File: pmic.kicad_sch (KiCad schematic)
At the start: 38 parts, among them J401 Conn_01x04, J402 EMI shield frame, U401 STPMIC1DPQR

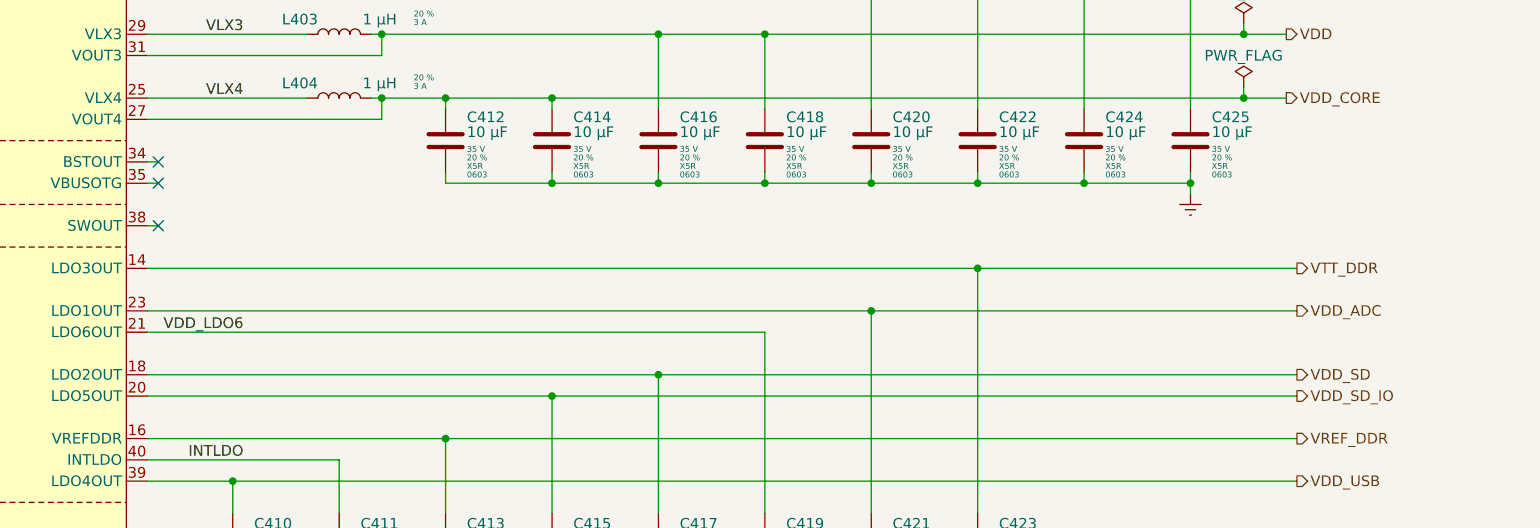
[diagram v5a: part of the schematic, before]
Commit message: Fallback to DDR series termination
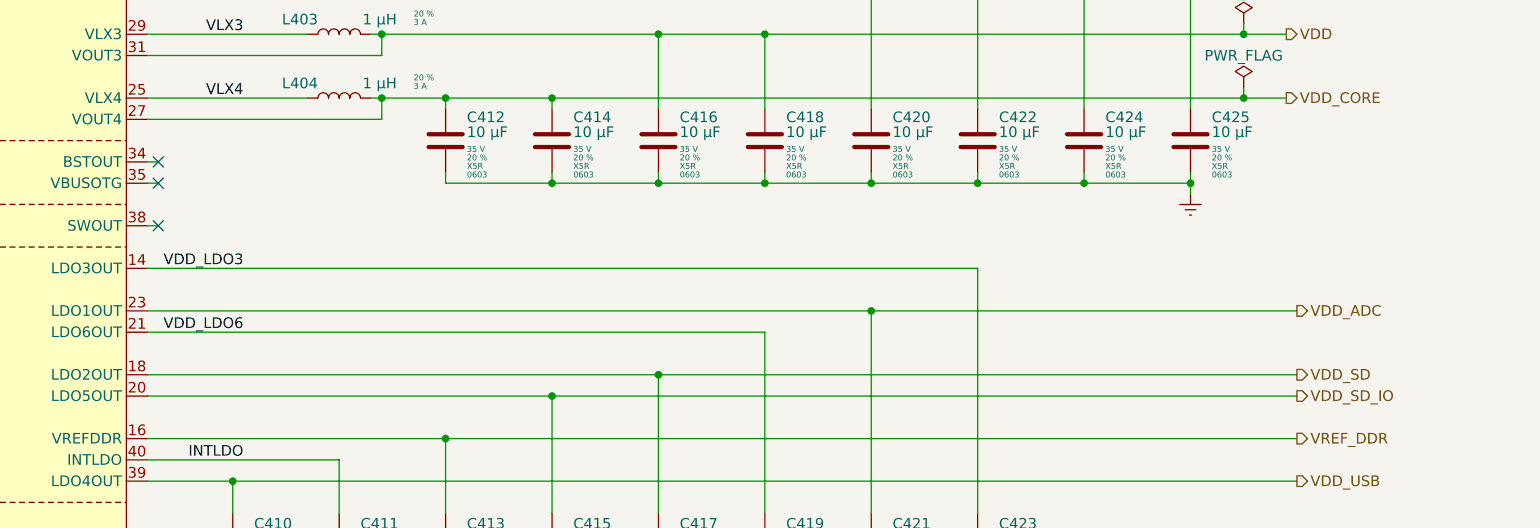
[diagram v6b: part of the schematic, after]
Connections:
- net VTT_DDR renamed VDD_LDO3
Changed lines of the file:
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@@
-	)
-	(junction
-		(at 292.1 157.48)
-		(diameter 0)
-		(color 0 0 0 0)
 	)
 	(junction
@@
 		(pts
 			(xy 133.35 114.3) (xy 133.35 116.84)
-		)
-		(stroke
-			(width 0)
-			(type default)
-		)
-	)
-	(wire
-		(pts
-			(xy 292.1 157.48) (xy 330.2 157.48)
 		)
 		(stroke
@@
 	(label "VLX2"
 		(at 204.47 121.92 180)
+		(effects
+			(font
+				(size 1.27 1.27)
+			)
+			(justify right bottom)
+		)
+	)
+	(label "VDD_LDO3"
+		(at 204.47 157.48 180)
 		(effects
 			(font
@@
 		(effects
 			(font
-				(size 1.27 1.27)
-			)
-			(justify left)
-		)
-	)
-	(hierarchical_label "VTT_DDR"
-		(shape output)
-		(at 330.2 157.48 0)
-		(effects
-			(font

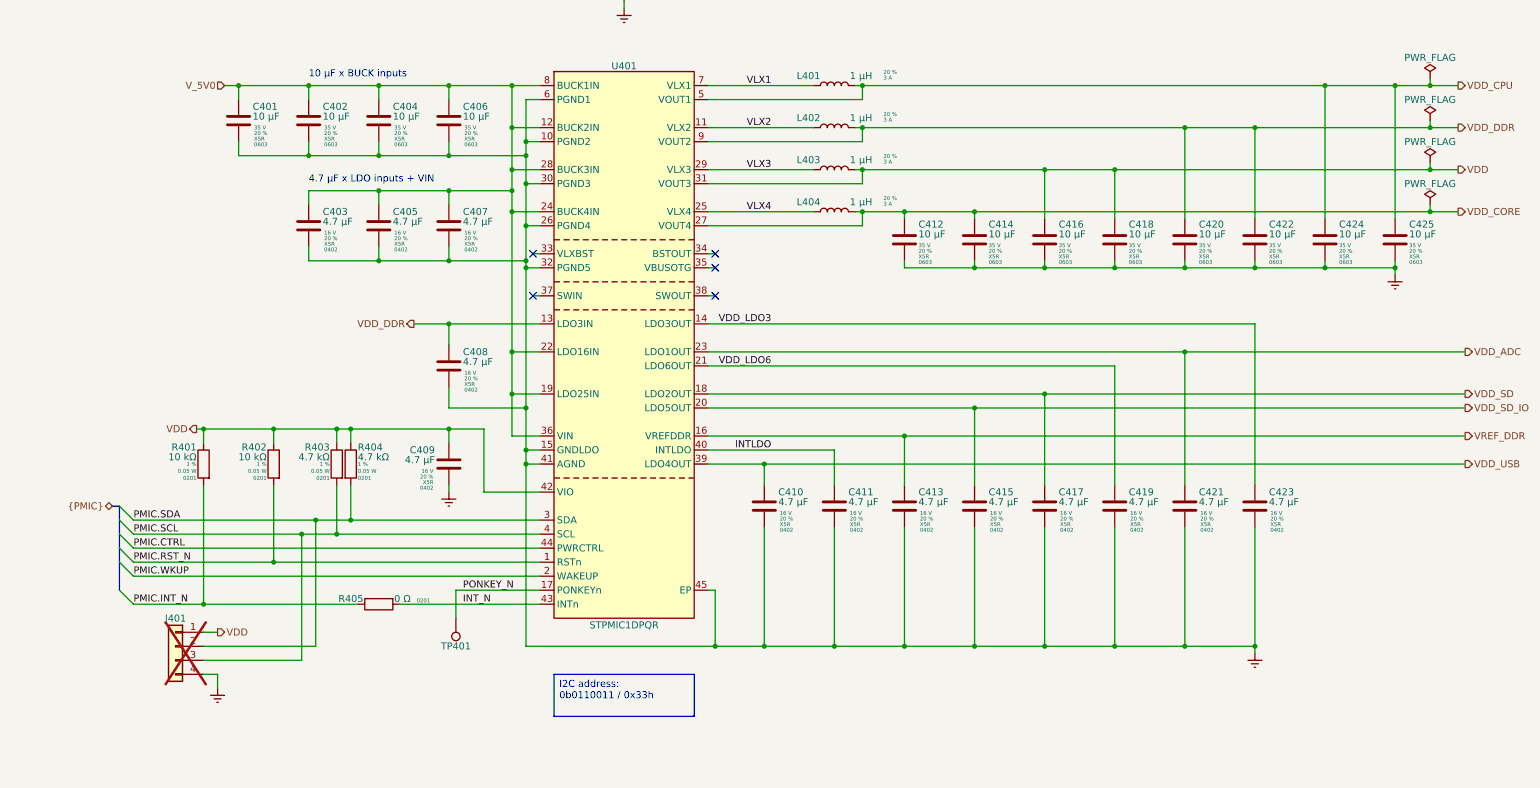
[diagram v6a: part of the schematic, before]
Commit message: Refactor MPU pinout and start routing interconnects
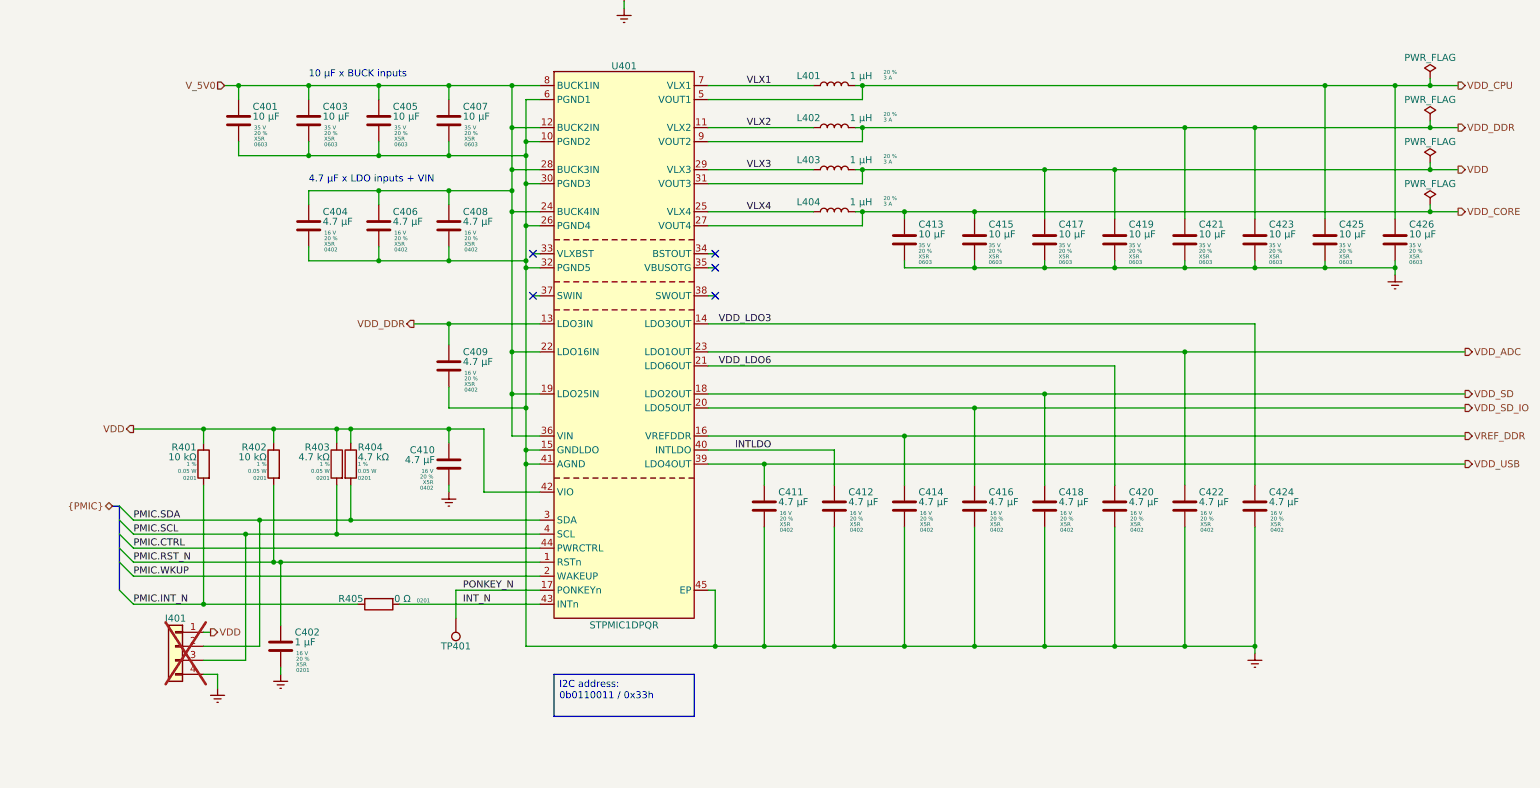
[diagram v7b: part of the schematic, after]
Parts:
- added C402: 1 µF, perfect_footprints:C_0201_0603Metric, symbol Device:C
- renumbered C402 to C403, C403 to C404, C404 to C405, C405 to C406, C406 to C407, C407 to C408, C408 to C409, C409 to C410, C410 to C411, C411 to C412, C412 to C413, C413 to C414, C414 to C415, C415 to C416, C416 to C417, C417 to C418, C418 to C419, C419 to C420, C420 to C421, C421 to C422, C422 to C423, C423 to C424, C424 to C425, C425 to C426
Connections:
- net GND: now also C402.2
- net PMIC.RST_N: now also C402.1
